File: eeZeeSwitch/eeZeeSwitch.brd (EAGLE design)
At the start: 15.7 x 7.6 mm, 6 parts

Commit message: Rev 0.1
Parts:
- removed SJ1: P'UP, SparkFun:SJ_2S-NO
- moved R1 2.30 mm to (10.7, 5.33), turned to 180 degrees
- moved S1 0.80 mm to (8.13, 2.54)
- moved JP1 0.51 mm to (14.5, 3.81), turned to 270 degrees
- moved C1 0.25 mm to (7.62, 2.54)
- turned JP2 to 270 degrees
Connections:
- net N$1: now also JP1.2; no longer SJ1.1
- net N$3: no longer JP1.2, SJ1.2
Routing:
- net N$3: track 10.8 -> 3.07 mm, vias 1 -> 0
- net N$1: track 7.76 -> 9.55 mm, vias 1 -> 0
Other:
- board size 15.7 x 7.6 mm -> 16.2 x 7.6 mm
- board text added: "VCC"
- board text removed: "P'UP"

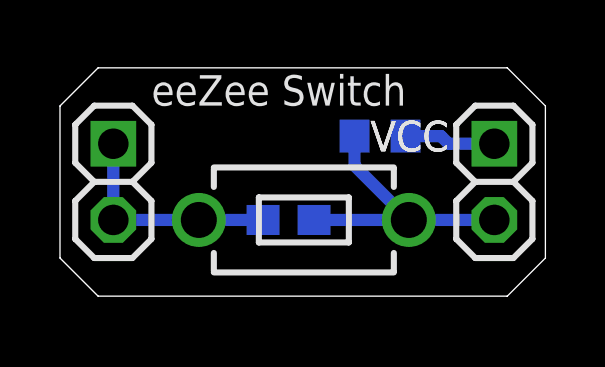
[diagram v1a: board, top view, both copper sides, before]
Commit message: Added debounce solder jumper so switch can be used as reset. Moved components and silkscreen around to accommodate.
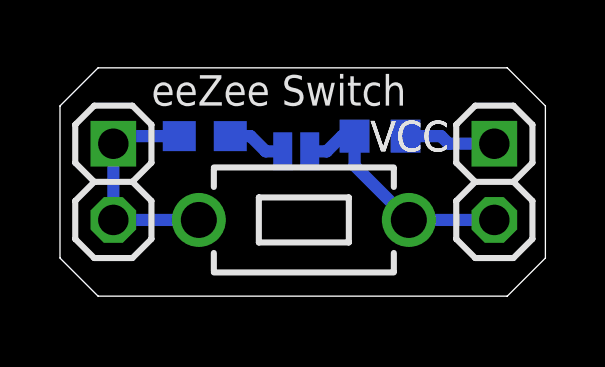
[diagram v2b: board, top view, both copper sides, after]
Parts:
- added SJ1: debounce, SparkFun:SJ_2S-NO
- moved C1 3.95 mm to (4.83, 5.33), turned to 0 degrees
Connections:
- new net N$4: C1.1, SJ1.1
- net N$1: now also SJ1.2; no longer C1.2
- net N$2: now also C1.2; no longer C1.1
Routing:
- net N$4: track 0.00 -> 1.96 mm
- net N$1: track 9.55 -> 8.10 mm
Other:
- board text added: "R0.2"
- board text added: "debounce"
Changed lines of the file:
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@@
 <layer number="19" name="Unrouted" color="6" fill="1" visible="yes" active="yes"/>
 <layer number="20" name="Dimension" color="15" fill="1" visible="yes" active="yes"/>
-<layer number="21" name="tPlace" color="7" fill="1" visible="yes" active="yes"/>
-<layer number="22" name="bPlace" color="7" fill="1" visible="yes" active="yes"/>
-<layer number="23" name="tOrigins" color="15" fill="1" visible="yes" active="yes"/>
-<layer number="24" name="bOrigins" color="15" fill="1" visible="yes" active="yes"/>
-<layer number="25" name="tNames" color="7" fill="1" visible="yes" active="yes"/>
-<layer number="26" name="bNames" color="7" fill="1" visible="yes" active="yes"/>
-<layer number="27" name="tValues" color="7" fill="1" visible="yes" active="yes"/>
-<layer number="28" name="bValues" color="7" fill="1" visible="yes" active="yes"/>
-<layer number="29" name="tStop" color="7" fill="3" visible="no" active="yes"/>
-<layer number="30" name="bStop" color="7" fill="6" visible="no" active="yes"/>
+<layer number="21" name="tPlace" color="7" fill="1" visible="no" active="yes"/>
+<layer number="22" name="bPlace" color="7" fill="1" visible="no" active="yes"/>
+<layer number="23" name="tOrigins" color="15" fill="1" visible="no" active="yes"/>
+<layer number="24" name="bOrigins" color="15" fill="1" visible="no" active="yes"/>
+<layer number="25" name="tNames" color="7" fill="1" visible="no" active="yes"/>
+<layer number="26" name="bNames" color="7" fill="1" visible="no" active="yes"/>
+<layer number="27" name="tValues" color="7" fill="1" visible="no" active="yes"/>
+<layer number="28" name="bValues" color="7" fill="1" visible="no" active="yes"/>
+<layer number="29" name="tStop" color="7" fill="3" visible="yes" active="yes"/>
+<layer number="30" name="bStop" color="7" fill="6" visible="yes" active="yes"/>
 <layer number="31" name="tCream" color="7" fill="4" visible="no" active="yes"/>
 <layer number="32" name="bCream" color="7" fill="5" visible="no" active="yes"/>
@@
 <wire x1="14.91" y1="7.61" x2="1.27" y2="7.61" width="0" layer="20"/>
 <wire x1="1.27" y1="7.61" x2="0" y2="6.34" width="0" layer="20"/>
-<text x="12.192" y="6.35" size="1.016" layer="22" font="vector" rot="MR0">ow.ly/qKUOk</text>
+<text x="12.7" y="0.508" size="1.016" layer="22" font="vector" rot="MR0">ow.ly/qKUOk</text>
 <text x="12.954" y="5.842" size="1.016" layer="21" font="vector" ratio="25" rot="R180">VCC</text>
+<text x="9.398" y="2.032" size="1.016" layer="26" font="vector" rot="MR0">R0.2</text>
 <text x="12.954" y="5.842" size="1.016" layer="121" font="vector" ratio="25" rot="R180">VCC</text>
 <wire x1="15.748" y1="5.715" x2="15.748" y2="4.445" width="0.2032" layer="121"/>
@@
 <wire x1="11.12799375" y1="4.239996875" x2="11.12799375" y2="3.639996875" width="0.2032" layer="121"/>
 <wire x1="11.12799375" y1="0.840003125" x2="11.12799375" y2="1.440003125" width="0.2032" layer="121"/>
-<text x="12.192" y="6.35" size="1.016" layer="122" font="vector" ratio="20" rot="MR0">ow.ly/qKUOk</text>
+<text x="12.7" y="0.508" size="1.016" layer="122" font="vector" ratio="20" rot="MR0">ow.ly/qKUOk</text>
+<wire x1="8.673996875" y1="5.825996875" x2="7.074003125" y2="5.825996875" width="0.2032" layer="122"/>
+<wire x1="8.673996875" y1="3.826003125" x2="8.87399375" y2="4.126" width="0.2032" layer="122" curve="89.999174"/>
+<wire x1="6.874003125" y1="4.126" x2="7.074003125" y2="3.826003125" width="0.2032" layer="122" curve="90.00124"/>
+<wire x1="7.074003125" y1="5.825996875" x2="6.874" y2="5.526" width="0.2032" layer="122" curve="90.000826"/>
+<wire x1="8.873996875" y1="5.526" x2="8.673996875" y2="5.825996875" width="0.2032" layer="122" curve="89.99876"/>
+<wire x1="7.074003125" y1="3.826003125" x2="8.673996875" y2="3.826003125" width="0.2032" layer="122"/>
+<text x="9.398" y="2.032" size="1.016" layer="122" font="vector" ratio="20" rot="MR0">R0.2</text>
 <text x="3.048" y="6.35" size="1.016" layer="121" font="vector" ratio="20">eeZee Switch</text>
-<text x="9.525" y="1.905" size="0.8128" layer="122" font="vector" ratio="25" rot="MR90">104</text>
-<text x="8.763" y="4.953" size="0.8128" layer="122" font="vector" ratio="25" rot="MR0">10K</text>
+<text x="3.937" y="4.572" size="0.8128" layer="122" font="vector" ratio="25" rot="MR180">104</text>
+<text x="9.779" y="4.572" size="0.8128" layer="122" font="vector" ratio="25" rot="MR180">10K</text>
+<text x="10.814" y="6.223" size="1.016" layer="122" font="vector" ratio="20" rot="MR0">debounce</text>
 </plain>
 <attributes>
@@
 </autorouter>
 <elements>
-<element name="C1" library="rcl" package="C0603" value="104" x="7.62" y="2.54" smashed="yes" rot="MR180">
-<attribute name="VALUE" x="9.525" y="1.905" size="0.8128" layer="28" rot="MR90"/>
+<element name="C1" library="rcl" package="C0603" value="104" x="4.826" y="5.334" smashed="yes" rot="MR0">
+<attribute name="VALUE" x="3.937" y="4.572" size="0.8128" layer="28" font="vector" rot="MR180"/>
 </element>
 <element name="R1" library="rcl" package="R0603" value="10K" x="10.668" y="5.334" smashed="yes" rot="MR180">
-<attribute name="VALUE" x="8.763" y="4.953" size="0.8128" layer="28" rot="MR0"/>
+<attribute name="VALUE" x="9.779" y="4.572" size="0.8128" layer="28" font="vector" rot="MR180"/>
 </element>
 <element name="JP1" library="pinhead-2" package="1X02-S" value="" x="14.478" y="3.81" smashed="yes" rot="R270">
@@
 <element name="S1" library="bt_electromech" package="6MMTACTILE_RECT" value="eeZee Switch" x="8.128" y="2.54" smashed="yes">
 <attribute name="VALUE" x="3.048" y="6.35" size="1.016" layer="27" font="vector"/>
+</element>
+<element name="SJ1" library="SparkFun" package="SJ_2S-NO" value="debounce" x="7.874" y="4.826" smashed="yes" rot="MR180">
+<attribute name="VALUE" x="10.814" y="6.223" size="1.016" layer="28" font="vector" rot="MR0"/>
 </element>
 </elements>
@@
 <signal name="N$1">
 <contactref element="R1" pad="1"/>
-<contactref element="C1" pad="2"/>
 <contactref element="S1" pad="P$2"/>
-<wire x1="8.47" y1="2.54" x2="11.628" y2="2.54" width="0.4064" layer="16"/>
 <contactref element="JP1" pad="2"/>
 <wire x1="11.628" y1="2.54" x2="14.478" y2="2.54" width="0.4064" layer="16"/>
 <wire x1="9.818" y1="5.334" x2="9.818" y2="4.35" width="0.4064" layer="16"/>
 <wire x1="9.818" y1="4.35" x2="11.628" y2="2.54" width="0.4064" layer="16"/>
+<contactref element="SJ1" pad="2"/>
+<wire x1="8.324" y1="4.826" x2="8.89" y2="4.826" width="0.4064" layer="16"/>
+<wire x1="8.89" y1="4.826" x2="9.398" y2="5.334" width="0.4064" layer="16"/>
+<wire x1="9.398" y1="5.334" x2="9.818" y2="5.334" width="0.4064" layer="16"/>
 </signal>
 <signal name="N$2">
 <contactref element="JP2" pad="2"/>
-<contactref element="C1" pad="1"/>
 <contactref element="JP2" pad="1"/>
 <wire x1="1.778" y1="5.08" x2="1.778" y2="2.54" width="0.4064" layer="16"/>
 <contactref element="S1" pad="P$1"/>
-<wire x1="6.77" y1="2.54" x2="4.628" y2="2.54" width="0.4064" layer="16"/>
 <wire x1="4.628" y1="2.54" x2="1.778" y2="2.54" width="0.4064" layer="16"/>
+<contactref element="C1" pad="2"/>
+<wire x1="3.976" y1="5.334" x2="2.032" y2="5.334" width="0.4064" layer="16"/>
+<wire x1="2.032" y1="5.334" x2="1.778" y2="5.08" width="0.4064" layer="16"/>
 </signal>
 <signal name="N$3">
@@
 <wire x1="12.7" y1="5.334" x2="11.518" y2="5.334" width="0.4064" layer="16"/>
 </signal>
+<signal name="N$4">
+<contactref element="SJ1" pad="1"/>
+<contactref element="C1" pad="1"/>
+<wire x1="5.676" y1="5.334" x2="6.35" y2="5.334" width="0.4064" layer="16"/>
+<wire x1="6.35" y1="5.334" x2="6.858" y2="4.826" width="0.4064" layer="16"/>
+<wire x1="6.858" y1="4.826" x2="7.424" y2="4.826" width="0.4064" layer="16"/>
+</signal>
 </signals>

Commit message: Revised circuit for easier optional debounce, revised silk for better usability.
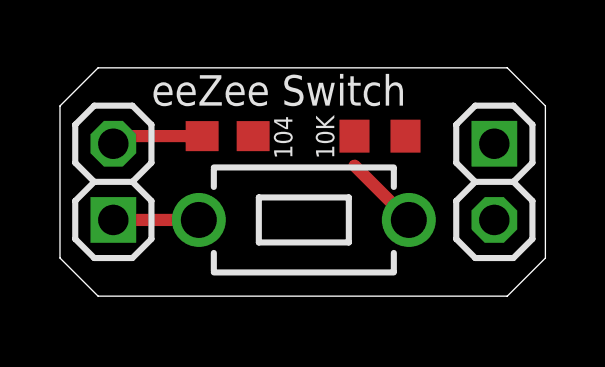
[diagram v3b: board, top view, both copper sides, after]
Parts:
- removed SJ1: debounce, SparkFun:SJ_2S-NO
- moved C1 0.76 mm to (5.59, 5.33), flipped to the top, turned to 180 degrees
- turned JP2 to 90 degrees
- flipped R1 to the top, turned to 0 degrees
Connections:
- removed net N$1: JP1.2, R1.1, S1.P$2, SJ1.2
- removed net N$2: C1.2, JP2.1, JP2.2, S1.P$1
- removed net N$3: JP1.1, R1.2
- removed net N$4: C1.1, SJ1.1
- new net DEBOUNCE: C1.2, JP2.2
- new net PULLUP: JP1.2, R1.2
- new net S1A: JP2.1, S1.P$1
- new net S1B: C1.1, JP1.1, R1.1, S1.P$2
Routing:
- net N$1: track 8.10 -> 0.00 mm
- net N$2: track 7.69 -> 0.00 mm
- net DEBOUNCE: track 0.00 -> 3.07 mm
- net N$3: track 3.07 -> 0.00 mm
- net S1B: track 0.00 -> 2.92 mm
- net S1A: track 0.00 -> 2.85 mm
- net N$4: track 1.96 -> 0.00 mm
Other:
- board text removed: "VCC"
- board text removed: "debounce"

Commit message: Final fixes to board
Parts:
- turned JP1 to 90 degrees
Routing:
- net S1B: track 2.92 -> 9.77 mm
- net PULLUP: track 0.00 -> 3.07 mm
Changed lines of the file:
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@@
 <layer number="21" name="tPlace" color="7" fill="1" visible="no" active="yes"/>
 <layer number="22" name="bPlace" color="7" fill="1" visible="no" active="yes"/>
-<layer number="23" name="tOrigins" color="15" fill="1" visible="no" active="yes"/>
+<layer number="23" name="tOrigins" color="15" fill="1" visible="yes" active="yes"/>
 <layer number="24" name="bOrigins" color="15" fill="1" visible="no" active="yes"/>
 <layer number="25" name="tNames" color="7" fill="1" visible="no" active="yes"/>
@@
 <attribute name="VALUE" x="9.144" y="4.572" size="0.6096" layer="27" font="vector" rot="R90"/>
 </element>
-<element name="JP1" library="pinhead-2" package="1X02-S" value="" x="14.478" y="3.81" smashed="yes" rot="R270">
-<attribute name="VALUE" x="11.303" y="6.35" size="1.27" layer="27" rot="R270"/>
+<element name="JP1" library="pinhead-2" package="1X02-S" value="" x="14.478" y="3.81" smashed="yes" rot="R90">
+<attribute name="VALUE" x="17.653" y="1.27" size="1.27" layer="27" rot="R90"/>
 </element>
 <element name="JP2" library="pinhead-2" package="1X02-S" value="" x="1.778" y="3.81" smashed="yes" rot="R90">
@@
 <wire x1="9.818" y1="4.35" x2="11.628" y2="2.54" width="0.4064" layer="1"/>
 <contactref element="JP1" pad="1"/>
-<wire x1="14.224" y1="5.334" x2="14.478" y2="5.08" width="0.4064" layer="1"/>
 <contactref element="R1" pad="1"/>
-<wire x1="11.628" y1="2.54" x2="14.224" y2="5.334" width="0" layer="19" extent="1-1"/>
-<wire x1="9.818" y1="5.334" x2="9.818" y2="4.35" width="0" layer="19" extent="1-1"/>
-<wire x1="6.438" y1="5.334" x2="9.818" y2="5.334" width="0" layer="19" extent="1-1"/>
+<wire x1="14.478" y1="2.54" x2="11.628" y2="2.54" width="0.4064" layer="1"/>
+<wire x1="9.818" y1="4.35" x2="9.818" y2="5.334" width="0.4064" layer="1"/>
+<wire x1="9.818" y1="5.334" x2="6.438" y2="5.334" width="0.4064" layer="1"/>
 </signal>
 <signal name="DEBOUNCE">
@@
 <contactref element="JP1" pad="2"/>
 <contactref element="R1" pad="2"/>
-<wire x1="11.518" y1="5.334" x2="14.478" y2="2.54" width="0" layer="19" extent="1-1"/>
+<wire x1="11.518" y1="5.334" x2="14.224" y2="5.334" width="0.4064" layer="1"/>
+<wire x1="14.224" y1="5.334" x2="14.478" y2="5.08" width="0.4064" layer="1"/>
 </signal>
 </signals>
